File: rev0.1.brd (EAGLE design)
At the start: 160 x 100 mm, 7 parts, among them U1 EFM32LG332F256G-E-QFP64, U2 FGPMMOPA6H, U3 NL-SW-LTE-GELS3-C

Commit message: made parts!
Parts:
- removed C1, C2, C3: .1uF, resistor:C0603
- removed R1: (no value), resistor:R0603
- added C4: (no value), resistor:C0402
- added IC1: MCP73811/2, adafruit:SOT23-5L
- added J2: (no value), SparkFun-Connectors:USB-MICROB
- added R2, R3: 4.7K, resistor:R0402
- added U4: TITAN-X1-GMS-3302, clackboard_lib:TITAN-X1-GMS-3302
- added U5: AT45DB161E-SHD2B-T, clackboard_lib:AT45DB161E-SHD2B-T
- added U6: LSM6DSL, clackboard_lib:LSM6DSL
- U1: value EFM32LG332F256G-E-QFP64 -> PIC24FJ128GB204; device clackboard_lib:EFM32LG332F256G-E-QFP64 -> clackboard_lib:PIC24FJ128GB204
- U2: value FGPMMOPA6H -> TELIT_RE866; device clackboard_lib:FGPMMOPA6H -> clackboard_lib:TELIT_RE866
- U3: value NL-SW-LTE-GELS3-C -> 24LC32A-SOT23-5; device clackboard_lib:NL-SW-LTE-GELS3-C -> clackboard_lib:24LC32A-SOT23-5
- moved U2 44.2 mm to (16.0, 53.0)
- moved U3 16.7 mm to (19.6, 37.3), turned to 180 degrees
- moved U1 10.3 mm to (10.0, 35.0), turned to 90 degrees
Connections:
- removed net +3V3: C1.1, C2.1, U2.1, U3.1
- new net 3.3V: C4.1, R2.2, R3.2, U3.4, U5.6
- new net CS: U5.4
- new net MISO: U5.8
- new net MOSI: U5.1
- new net RESET: U5.3
- new net SCK: U5.2
- new net SCL: R2.1, U1.24, U3.1, U6.13
- new net SDA: R3.1, U1.23, U3.3, U6.14
- new net USB_N: J2.D-, U1.9
- new net USB_P: J2.D+, U1.8
- new net VDD: IC1.4
- new net VSS: IC1.2
- new net V_USB: J2.VBUS
- new net WP: U5.5
- net GND: now also C4.2, J2.GND, J2.MT1, J2.MT2, J2.P$1, J2.P$2, U1.16, U1.29, U1.39, U2.C3, U2.D1, U2.D2, U2.E3, U2.F1, U2.F2, U2.F3, U2.F6, U2.G1, U2.G3, U3.2, U3.5, U4.1, U4.10, U4.11, U4.24, U4.3, U4.4, U4.5, U4.6, U4.9, U5.7, U6.1, U6.6, U6.7; no longer C1.2, C2.2, U2.12, U2.19, U2.3, U2.8, U3.10, U3.11, U3.15, U3.4
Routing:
- net USB_P: track 0.00 -> 16.6 mm
- net USB_N: track 0.00 -> 16.5 mm
- net SCL: track 0.00 -> 13.3 mm, vias 0 -> 1
- net SDA: track 0.00 -> 12.7 mm, vias 0 -> 1
- net 3.3V: track 0.00 -> 3.78 mm
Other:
- board size 160 x 100 mm -> 30.5 x 69.2 mm
- board text added: "ANT"
- board text added: "GPS"
- board text added: "SIM CARD"
- board text added: "button"
- board text added: "usb"

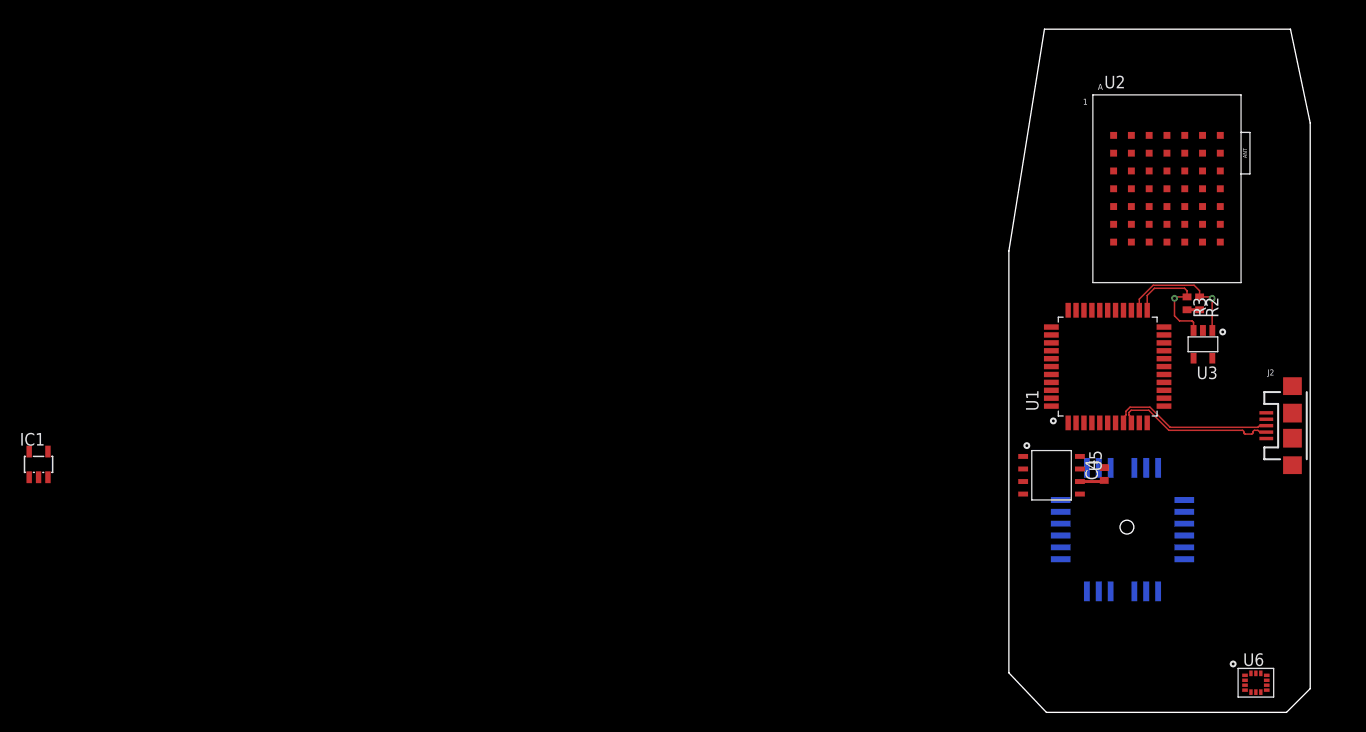
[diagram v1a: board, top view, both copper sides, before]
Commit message: added bat management
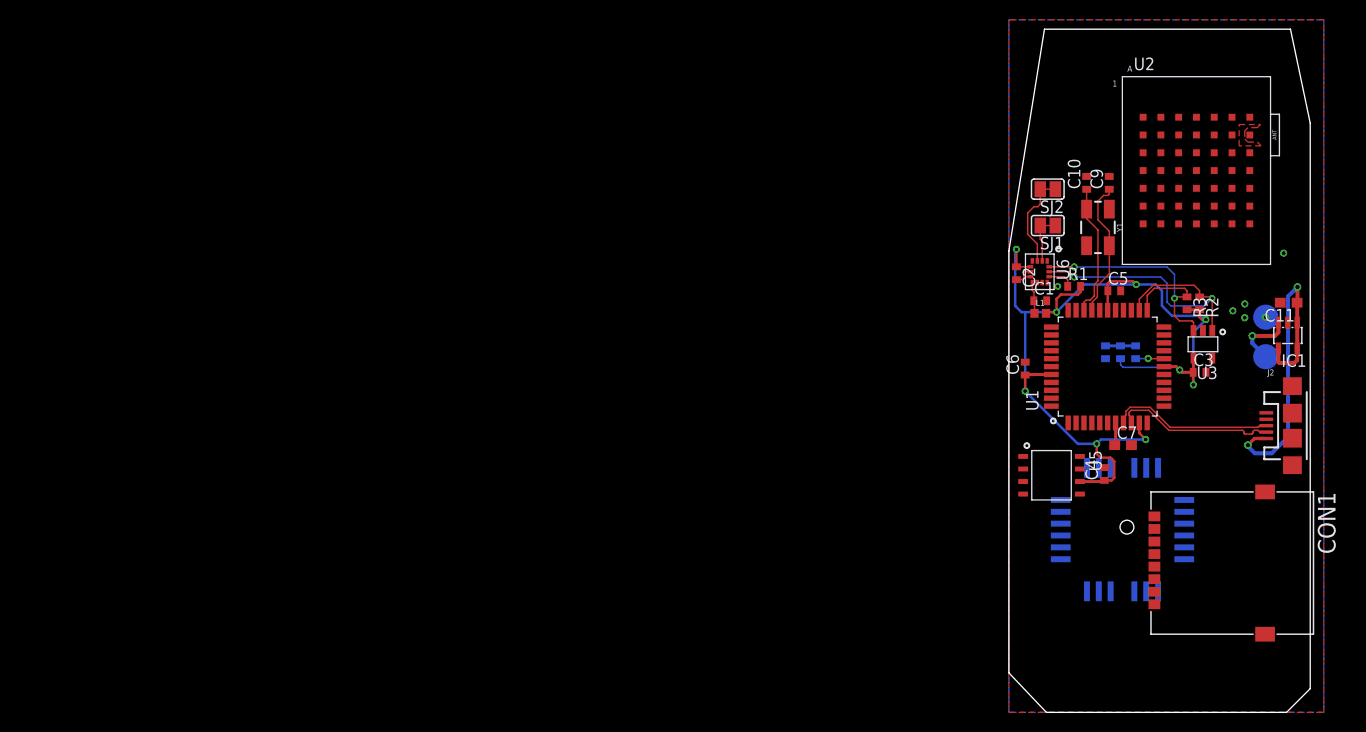
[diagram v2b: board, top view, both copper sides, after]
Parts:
- added BAT+, BAT-: PTR1B2,54, testpad:B2,54
- added C1, C2, C3, C5, C6, C8: 0.1uF, resistor:C0402
- added C10, C9: 22pF, resistor:C0402
- added C11: 1uF, resistor:C0603
- added C7: 10uF, resistor:C0603
- added CON1: SIMCARD_HOLDER_693022010811, clackboard_lib:SIMCARD_HOLDER_693022010811
- added L1: MPZ1608D300BTA00, SparkFun-Coils:0402
- added R1, R5: 10K, resistor:R0402
- added R4: 100R, resistor:R0402
- added SJ1, SJ2: (no value), jumper:SJ
- added Y1: 16MHz, SparkFun-Clocks:CRYSTAL-SMD-5X3.2-4PAD
- C4: value (none) -> 0.1uF
- moved IC1 127.1 mm to (28.2, 38.1), turned to 180 degrees
- moved U6 47.0 mm to (3.13, 44.6), turned to 270 degrees
- moved U2 3.51 mm to (19.0, 54.8)
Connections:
- removed net VDD: IC1.4
- removed net VSS: IC1.2
- new net INT1: U6.4
- new net INT2: U6.9
- new net MCLR: R4.2, U1.18
- new net N$1: SJ1.2, U6.2
- new net N$2: SJ2.2, U6.3
- new net N$3: R1.1, U6.12
- new net N$5: C1.1, L1.1, U6.8
- new net N$6: C8.1, R4.1, R5.1
- new net N$7: C9.1, U1.30, Y1.3
- new net N$8: C10.1, U1.31, Y1.1
- new net N$9: C7.1, U1.7
- new net RX0: U4.20
- new net TX0: U4.19
- new net VBAT: BAT+.TP, IC1.3
- net 3.3V: now also C2.1, C3.1, C5.1, C6.1, L1.2, R1.2, R5.2, U1.10, U1.17, U1.28, U1.40, U6.5
- net GND: now also BAT-.TP, C1.2, C10.2, C11.2, C2.2, C3.2, C5.2, C6.2, C7.2, C8.2, C9.2, CON1.P$10, CON1.P$9, IC1.2, SJ1.1, SJ2.1
- net V_USB: now also C11.1, IC1.1, IC1.4, IC1.5
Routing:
- net 3.3V: track 3.78 -> 103.5 mm, vias 0 -> 9
- net V_USB: track 0.00 -> 33.7 mm, vias 0 -> 2
- net SCL: track 13.3 -> 32.6 mm, vias 1 -> 2
- net SDA: track 12.7 -> 28.1 mm, vias 1 -> 2
- net N$7: track 0.00 -> 14.2 mm
- net N$8: track 0.00 -> 13.5 mm
- net N$2: track 0.00 -> 8.41 mm
- net VBAT: track 0.00 -> 6.44 mm, vias 0 -> 1
- net GND: track 0.00 -> 5.86 mm, vias 0 -> 6
- net N$1: track 0.00 -> 3.66 mm
- net N$5: track 0.00 -> 3.21 mm
- net N$6: track 0.00 -> 3.05 mm
- net MCLR: track 0.00 -> 2.88 mm, vias 0 -> 1
- net N$3: track 0.00 -> 2.66 mm
- net N$9: track 0.00 -> 2.29 mm
- added copper zone on layer 1, net GND
- added copper zone on layer 16, net GND
- added copper zone on layer 1, net N$4

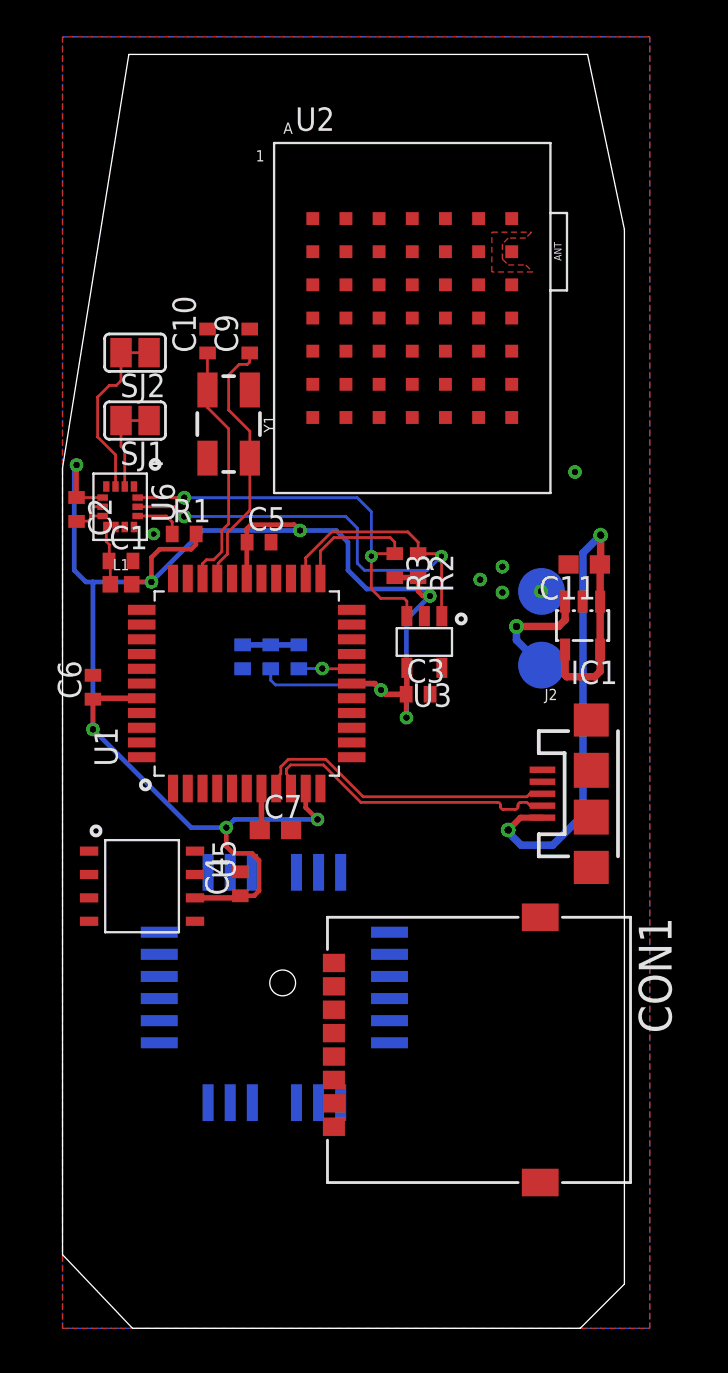
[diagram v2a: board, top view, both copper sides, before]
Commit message: reroute with new component placements
had a redo on the component placement for better routability, changed the battery charging circuit, still need to confirm which pins for communications go to the PIC. need to still add button.
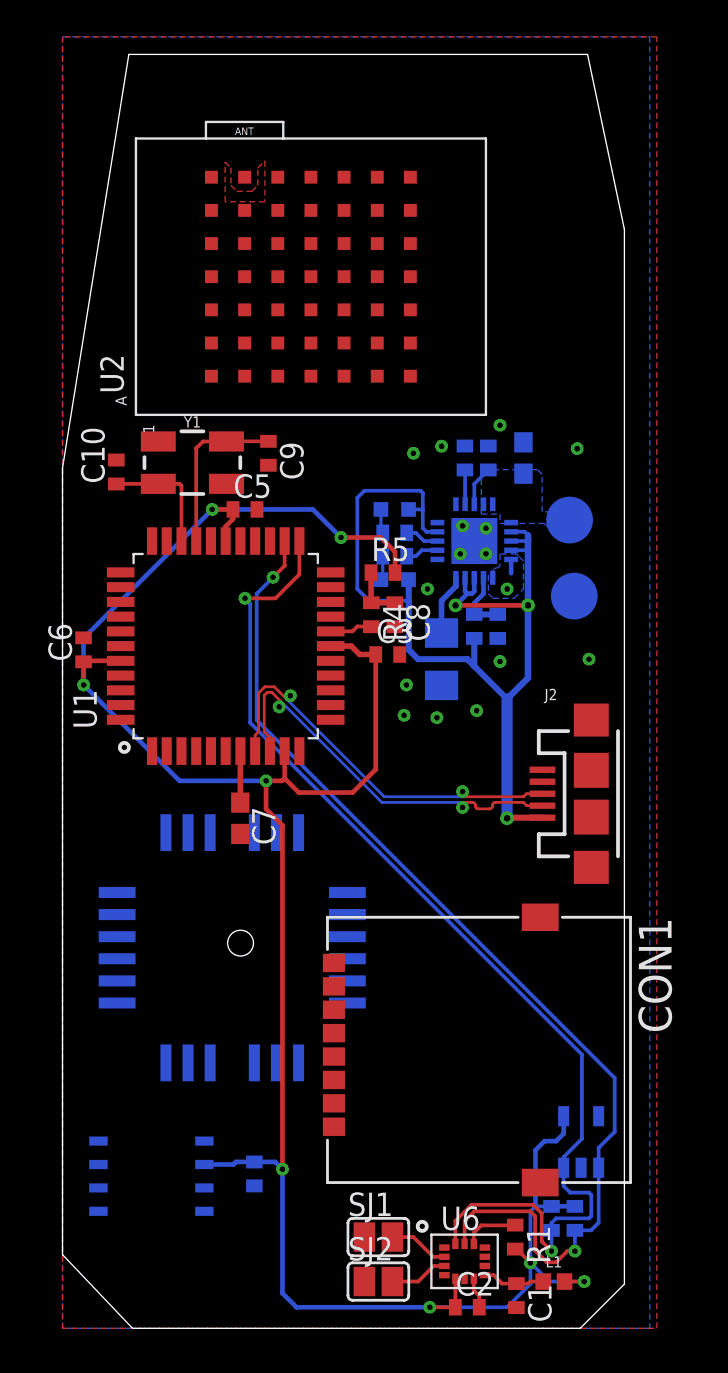
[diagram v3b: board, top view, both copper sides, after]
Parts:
- removed C11: 1uF, resistor:C0603
- removed IC1: MCP73811/2, adafruit:SOT23-5L
- added C12: 10uF, resistor:C0603
- added F1: 15K, adafruit:R1206
- added IC2: MCP73871, adafruit:QFN20
- added LED1: GREEN, adafruit:CHIP-LED0603
- added LED2: ORANGE, adafruit:CHIP-LED0603
- added R10, R7: 100K, resistor:R0402
- added R11, R8, R9: 1K, resistor:R0402
- added R6: 270K, resistor:R0402
- moved SJ2 52.1 mm to (17.1, 2.54), turned to 0 degrees
- moved C2 48.2 mm to (22.0, 1.14), turned to 0 degrees
- moved SJ1 46.2 mm to (17.1, 4.95), turned to 0 degrees
- moved C1 45.3 mm to (24.6, 1.78), turned to 270 degrees
- moved U6 45.0 mm to (21.8, 3.63), turned to 0 degrees
- moved L1 44.5 mm to (26.7, 2.54)
- moved R1 42.2 mm to (24.6, 4.95), turned to 270 degrees
- moved R2 36.4 mm to (27.8, 5.97), flipped to the bottom, turned to 90 degrees
- moved R3 36.4 mm to (26.5, 5.97), flipped to the bottom, turned to 90 degrees
- moved U3 28.4 mm to (28.2, 10.1), flipped to the bottom, turned to 0 degrees
- moved C4 15.8 mm to (10.4, 8.38), flipped to the bottom, turned to 270 degrees
- moved U5 15.8 mm to (4.83, 8.26), flipped to the bottom, turned to 90 degrees
- moved C10 8.67 mm to (2.92, 46.5)
- moved C8 8.57 mm to (18.0, 38.7), flipped to the top
- moved BAT+ 8.02 mm to (27.5, 43.9)
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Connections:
- new net 5V: IC2.1, IC2.20
- new net N$10: IC2.2, R6.1, R7.2
- new net N$13: LED1.C, R8.2
- new net N$14: LED2.C, R9.2
- new net N$15: IC2.7, R8.1
- new net N$16: IC2.8, R9.1
- new net N$19: IC2.12, R10.2
- new net N$20: IC2.13, R11.2
- new net N$24: F1.1, IC2.5
- net GND: now also C12.2, F1.2, IC2.10, IC2.11, R10.1, R11.1, R7.1; no longer C11.2, IC1.2
- net VBAT: now also C12.1, IC2.14, IC2.15, IC2.16; no longer IC1.3
- net V_USB: now also IC2.17, IC2.18, IC2.19, IC2.3, IC2.4, IC2.9, LED1.A, LED2.A, R6.2; no longer C11.1, IC1.1, IC1.4, IC1.5
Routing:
- net SDA: track 28.1 -> 60.6 mm
- net SCL: track 32.6 -> 58.6 mm
- net 3.3V: track 103.5 -> 127.8 mm, vias 9 -> 8
- net V_USB: track 33.7 -> 54.7 mm, vias 2 -> 3
- net N$8: track 13.5 -> 6.59 mm
- net VBAT: track 6.44 -> 0.00 mm, vias 1 -> 0
- net USB_N: track 16.5 -> 22.3 mm, vias 0 -> 2
- net USB_P: track 16.6 -> 22.4 mm, vias 0 -> 2
- net N$2: track 8.41 -> 3.17 mm
- net N$7: track 14.2 -> 9.11 mm
- net GND: track 5.86 -> 1.66 mm, vias 6 -> 15
- net N$10: track 0.00 -> 3.46 mm
- net N$24: track 0.00 -> 3.31 mm
- net N$20: track 0.00 -> 2.17 mm
- net N$19: track 0.00 -> 1.86 mm
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- added copper zone on layer 16, net 5V
- added copper zone on layer 16, net VBAT

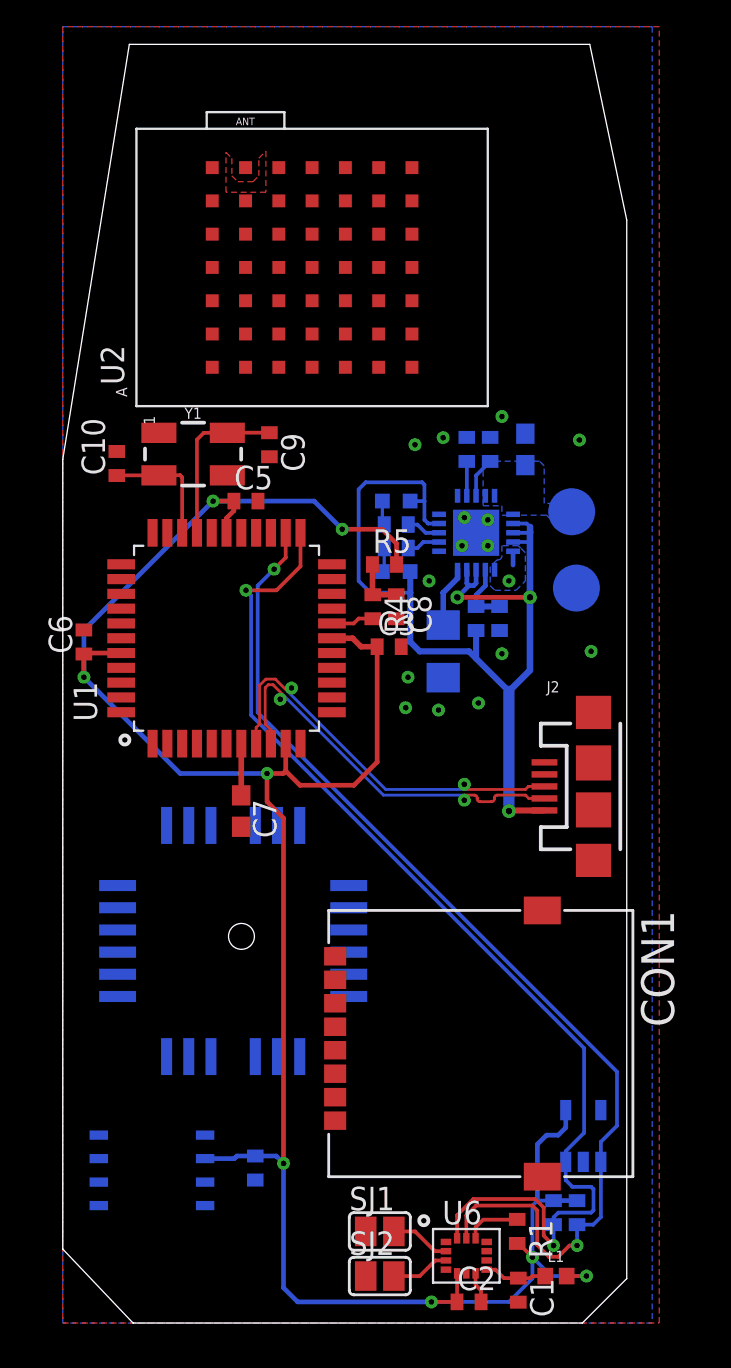
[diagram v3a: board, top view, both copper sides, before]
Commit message: routed for PIC for cleaner routing
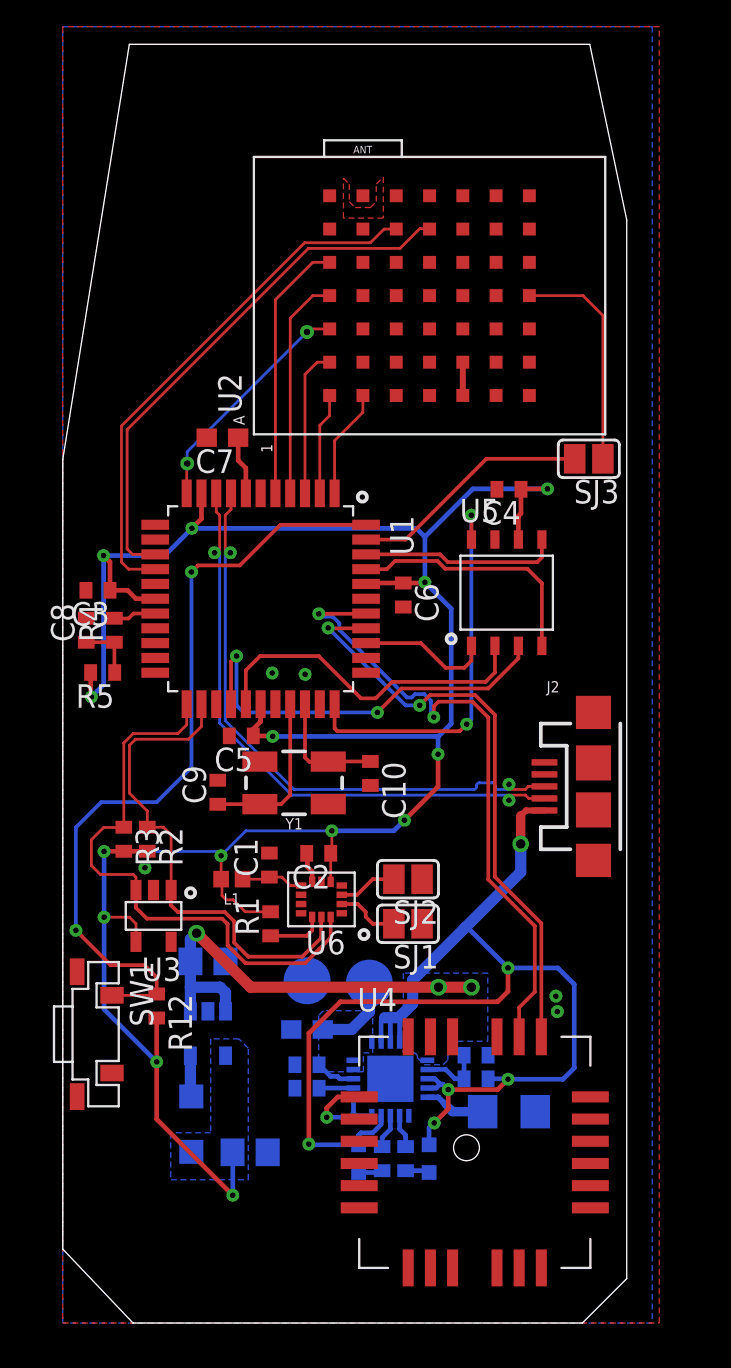
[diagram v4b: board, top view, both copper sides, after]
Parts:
- removed CON1: SIMCARD_HOLDER_693022010811, clackboard_lib:SIMCARD_HOLDER_693022010811
- added C11, C13: 10uF, resistor:C0805
- added L2: 4.7µH/±30%/1.2A, SparkFun-Coils:INDUCTOR_4.7UH
- added R12: 10K, resistor:R0402
- added SJ3: (no value), jumper:SJ
- added SW1: BUTTON-TL3330AF130QG, clackboard_lib:BUTTON-TL3330AF130QG
- added U7: PAM2305AAB330, clackboard_lib:PAM2305AAB330
- moved C4 39.2 mm to (24.1, 45.1), flipped to the top, turned to 180 degrees
- moved U5 36.7 mm to (24.0, 39.5), flipped to the top, turned to 0 degrees
- moved LED2 35.6 mm to (16.0, 8.89), turned to 180 degrees
- moved R10 35.6 mm to (13.2, 12.7), turned to 180 degrees
- moved R11 34.7 mm to (13.2, 14.0), turned to 180 degrees
- moved R9 34.3 mm to (17.3, 8.89), turned to 270 degrees
- moved C12 33.5 mm to (13.2, 15.9), turned to 0 degrees
- moved R8 33.0 mm to (18.5, 8.89), turned to 270 degrees
- moved LED1 31.8 mm to (19.8, 8.89), turned to 180 degrees
- moved R2 30.8 mm to (4.57, 26.2), flipped to the top, turned to 270 degrees
- moved R3 30.8 mm to (3.30, 26.2), flipped to the top, turned to 270 degrees
- moved IC2 29.9 mm to (17.7, 13.2), turned to 0 degrees
- moved BAT+ 27.7 mm to (16.6, 18.4), turned to 270 degrees
- moved L1 27.7 mm to (9.14, 24.0), turned to 180 degrees
- moved C1 26.6 mm to (11.2, 24.8), turned to 90 degrees
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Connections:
- new net BOOT0: U1.15, U2.C6
- new net BUTTON: R12.1, SW1.SW1, U1.44
- new net IUR_IN: U1.3, U2.A2
- new net IUR_OUT: U1.11, U2.A3
- new net N$11: U4.7
- new net N$12: U2.E1, U2.E2
- new net N$17: L2.P$1, U7.5
- new net N$18: SJ3.1, U2.G4
- new net PGC: U1.22
- new net PGD: U1.21
- new net PIC_CTS: U1.2, U2.A1
- new net PIC_RTS: U1.1, U2.B1
- new net PIC_RX: U1.4, U2.A4
- new net PIC_TX: U1.5, U2.A5
- new net TELIT_RESET: SJ3.2, U1.43
- new net TESTMODE: U1.14, U2.D6
- net 3.3V: now also C13.1, L2.P$2, R12.2, U7.4
- net 5V: now also C11.1, U7.1, U7.3
- net CS: now also U1.41
- net GND: now also C11.2, C13.2, SW1.MNT@1, SW1.MNT@2, SW1.SW2, U7.2; no longer CON1.P$10, CON1.P$9
- net MISO: now also U1.33
- net MOSI: now also U1.36
- net RESET: now also U1.26
- net RX0: now also U1.38
- net SCK: now also U1.27
- net TX0: now also U1.37
- net WP: now also U1.42
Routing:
- net BUTTON: track 0.00 -> 43.0 mm, vias 0 -> 2
- net RX0: track 0.00 -> 34.5 mm, vias 0 -> 2
- net TX0: track 0.00 -> 31.9 mm, vias 0 -> 2
- net SCL: track 58.6 -> 27.1 mm, vias 2 -> 0
- net SDA: track 60.6 -> 31.4 mm, vias 2 -> 0
- net TESTMODE: track 0.00 -> 29.0 mm
- net BOOT0: track 0.00 -> 28.6 mm
- net 5V: track 0.75 -> 23.5 mm, vias 1 -> 3
- net RESET: track 0.00 -> 22.7 mm, vias 0 -> 2
- net MISO: track 0.00 -> 21.4 mm, vias 0 -> 2
- net SCK: track 0.00 -> 18.6 mm
- net V_USB: track 54.7 -> 70.2 mm, vias 3 -> 6
- net PIC_TX: track 0.00 -> 14.2 mm
- net CS: track 0.00 -> 13.6 mm
- net TELIT_RESET: track 0.00 -> 13.1 mm
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- added copper zone on layer 16, net 3.3V
